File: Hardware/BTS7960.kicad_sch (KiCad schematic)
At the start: 29 parts, among them J10 Screw_Terminal_01x04, J11 Screw_Terminal_01x04, J4 Screw_Terminal_01x04, U7 HCPL-2631, U8 HCPL-2631

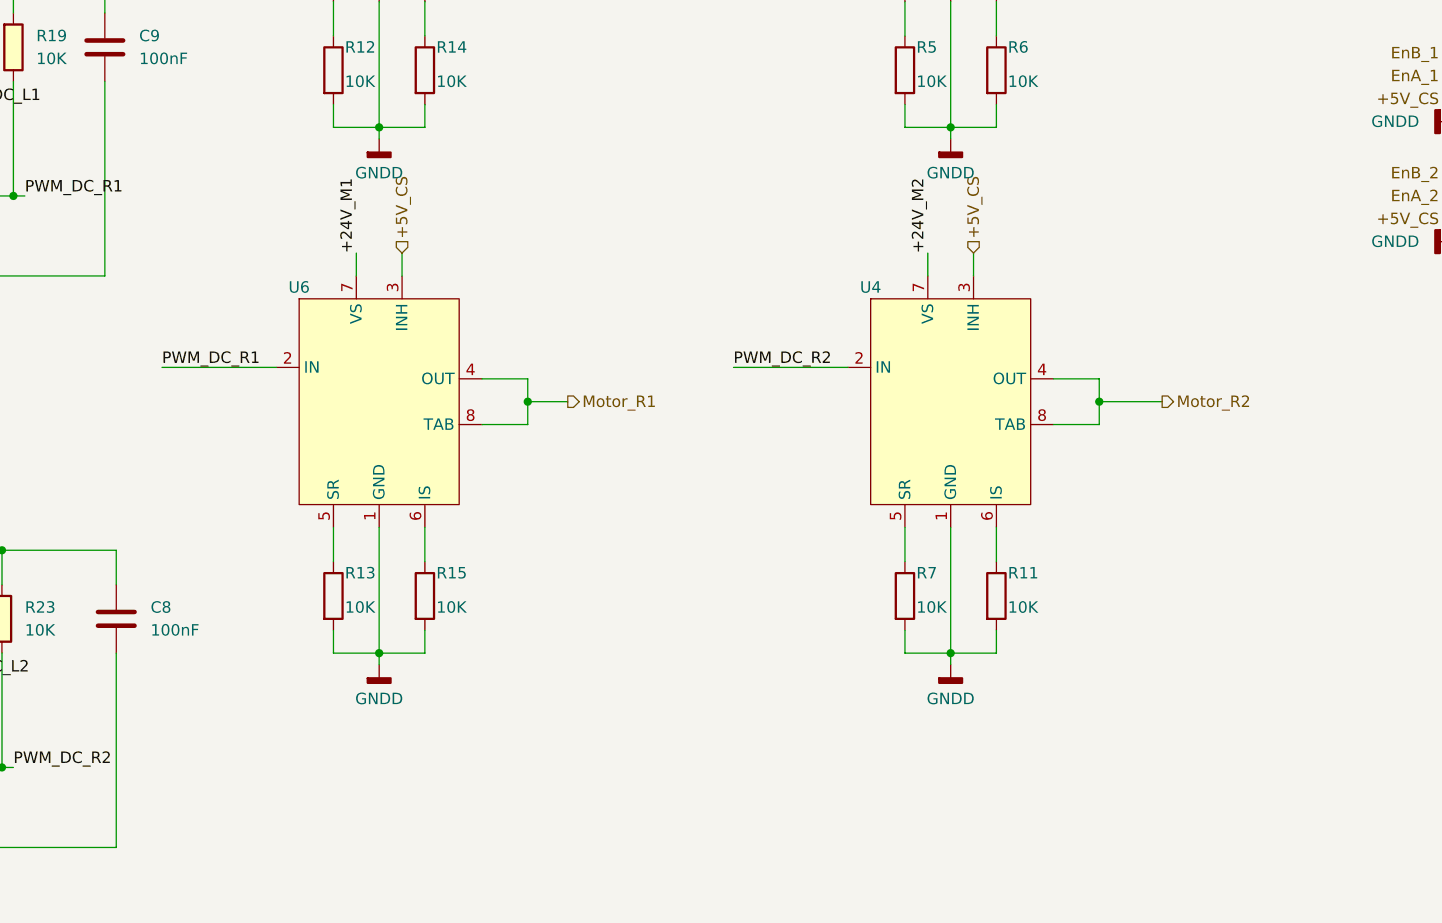
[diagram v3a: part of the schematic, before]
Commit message: Update schematic part2
Vẽ bus dành cho khối BLDC
Đóng khối chức năng cho sheet MCT8316
Tạo sheet nguồn cho các mạch nguồn Buck DCDC, LDO LD1117, BS0505
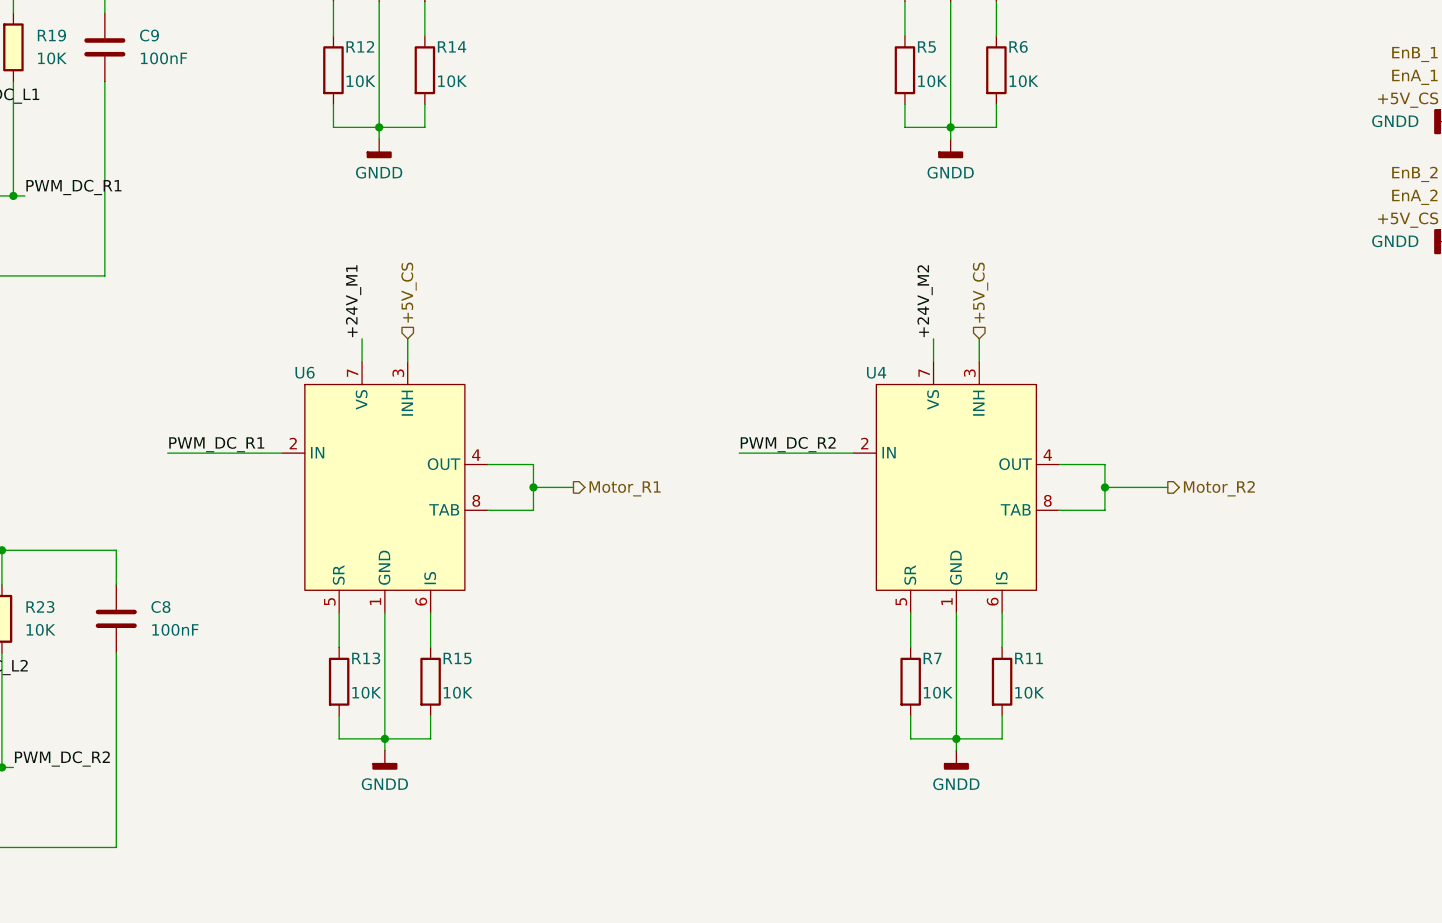
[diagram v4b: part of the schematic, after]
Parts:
- J10, J11: footprint Connector_PinHeader_2.54mm:PinHeader_1x04_P2.54mm_Vertical -> IVS_FOOTPRINTS:Conn-Vert-THT-4P-2.54mm-S4B_XH_SM4_TB
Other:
- moved on the sheet: R11, R13, R15, R7, U4, U6

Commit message: Add PCB
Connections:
- net MCU_PWM_L1: now also R16.1; no longer R17.1
- net MCU_PWM_R1: now also R17.1; no longer R16.1
- net PWM_DC_L1: now also R19.2, U7.6 (VO2); no longer R18.2, U7.7 (VO1)
- net PWM_DC_R1: now also R18.2, U7.7 (VO1); no longer R19.2, U7.6 (VO2)
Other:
- note added: "Driver Motor DC"
- note added: "Input Encoder"
- note added: "Isolation"
- note added: "Output Motor"
- moved on the sheet: C8, C9, F3, F4, J10, J11, J4, R11, R12, R13, R14, R15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

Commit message: Layout PCB
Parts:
- J4: footprint TerminalBlock:TerminalBlock_bornier-4_P5.08mm -> IVS_FOOTPRINTS:TerminalBlock_bornier-4_P5.08mm
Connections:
- net EnA_1 renamed En.EnA_1
- net EnA_2 renamed En.EnA_2
- net EnB_1 renamed En.EnB_1
- net EnB_2 renamed En.EnB_2
- net MCU_PWM_L1 renamed BTS.PWM_L1
- net MCU_PWM_L2 renamed BTS.PWM_L2
- net MCU_PWM_R1 renamed BTS.PWM_R1
- net MCU_PWM_R2 renamed BTS.PWM_R2
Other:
- moved on the sheet: C8, C9, F3, F4, R11, R12, R13, R14, R15, R16, R17, R18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

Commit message: Update Encoder
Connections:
- net +5V_CS: no longer J10.3 (Pin_3), J11.3 (Pin_3)
- net GND: now also J10.4 (Pin_4), J11.4 (Pin_4)
- net GNDD: no longer J10.4 (Pin_4), J11.4 (Pin_4)
- new net +3V3_MCU: J10.3 (Pin_3), J11.3 (Pin_3)
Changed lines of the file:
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@@
     (effects (font (size 1.27 1.27)) (justify left))
-  )
-  (hierarchical_label "+5V_CS" (shape input) (at 121.92 180.975 180) (fields_autoplaced)
-    (effects (font (size 1.27 1.27)) (justify right))
   )
   (hierarchical_label "En{En}" (shape output) (at 140.97 44.45 0) (fields_autoplaced)
@@
     (effects (font (size 1.27 1.27)) (justify left))
   )
+  (hierarchical_label "+3V3_MCU" (shape input) (at 121.92 180.975 180) (fields_autoplaced)
+    (effects (font (size 1.27 1.27)) (justify right))
+  )
   (hierarchical_label "+5V_CS" (shape input) (at 60.325 88.265 90) (fields_autoplaced)
     (effects (font (size 1.27 1.27)) (justify left))
@@
     (effects (font (size 1.27 1.27)) (justify left))
   )
-  (hierarchical_label "+5V_CS" (shape input) (at 121.92 167.64 180) (fields_autoplaced)
+  (hierarchical_label "+3V3_MCU" (shape input) (at 121.92 167.64 180) (fields_autoplaced)
     (effects (font (size 1.27 1.27)) (justify right))
   )
@@
     )
   )
+  (symbol (lib_id "power:GND") (at 121.92 183.515 270) (unit 1)
+    (in_bom yes) (on_board yes) (dnp no) (fields_autoplaced)
+    (property "Reference" "#PWR051" (at 115.57 183.515 0)
+      (effects (font (size 1.27 1.27)) hide)
+    )
+    (property "Value" "GND" (at 118.11 183.515 90)
+      (effects (font (size 1.27 1.27)) (justify right))
+    )
+    (property "Footprint" "" (at 121.92 183.515 0)
+      (effects (font (size 1.27 1.27)) hide)
+    )
+    (property "Datasheet" "" (at 121.92 183.515 0)
+      (effects (font (size 1.27 1.27)) hide)
+    )
+    (pin "1")
+    (instances
+      (project "DriverMotor"
+        (path "/8a82bd86-ff43-47ee-a4c0-46ff08914251/69bbd6ce-e9d0-4e66-98e2-7e43c19203ad"
+          (reference "#PWR051") (unit 1)
+        )
+      )
+    )
+  )
   (symbol (lib_name "BTS7960_2") (lib_id "IVS_SYMBOLS:BTS7960") (at 248.285 47.625 0) (unit 1)
     (in_bom yes) (on_board yes) (dnp no)
@@
     )
   )
-  (symbol (lib_id "power:GNDD") (at 121.92 183.515 270) (unit 1)
-    (in_bom yes) (on_board yes) (dnp no) (fields_autoplaced)
-    (property "Reference" "#PWR052" (at 115.57 183.515 0)
-      (effects (font (size 1.27 1.27)) hide)
-    )
-    (property "Value" "GNDD" (at 118.11 183.515 90)
-      (effects (font (size 1.27 1.27)) (justify right))
-    )
-    (property "Footprint" "" (at 121.92 183.515 0)
-      (effects (font (size 1.27 1.27)) hide)
-    )
-    (property "Datasheet" "" (at 121.92 183.515 0)
-      (effects (font (size 1.27 1.27)) hide)
-    )
-    (pin "1")
-    (instances
-      (project "DriverMotor"
-        (path "/8a82bd86-ff43-47ee-a4c0-46ff08914251/69bbd6ce-e9d0-4e66-98e2-7e43c19203ad"
-          (reference "#PWR052") (unit 1)
-        )
-      )
-    )
-  )
   (symbol (lib_id "power:GND") (at 50.165 50.165 270) (unit 1)
     (in_bom yes) (on_board yes) (dnp no) (fields_autoplaced)
@@
         (path "/8a82bd86-ff43-47ee-a4c0-46ff08914251/69bbd6ce-e9d0-4e66-98e2-7e43c19203ad"
           (reference "R19") (unit 1)
+        )
+      )
+    )
+  )
+  (symbol (lib_id "power:GND") (at 121.92 170.18 270) (unit 1)
+    (in_bom yes) (on_board yes) (dnp no) (fields_autoplaced)
+    (property "Reference" "#PWR047" (at 115.57 170.18 0)
+      (effects (font (size 1.27 1.27)) hide)
+    )
+    (property "Value" "GND" (at 118.11 170.18 90)
+      (effects (font (size 1.27 1.27)) (justify right))
+    )
+    (property "Footprint" "" (at 121.92 170.18 0)
+      (effects (font (size 1.27 1.27)) hide)
+    )
+    (property "Datasheet" "" (at 121.92 170.18 0)
+      (effects (font (size 1.27 1.27)) hide)
+    )
+    (pin "1")
+    (instances
+      (project "DriverMotor"
+        (path "/8a82bd86-ff43-47ee-a4c0-46ff08914251/69bbd6ce-e9d0-4e66-98e2-7e43c19203ad"
+          (reference "#PWR047") (unit 1)
         )
       )
@@
         )
       )
-    )
-  )
-  (symbol (lib_id "power:GNDD") (at 121.92 170.18 270) (unit 1)
-    (in_bom yes) (on_board yes) (dnp no) (fields_autoplaced)
-    (property "Reference" "#PWR051" (at 115.57 170.18 0)
-      (effects (font (size 1.27 1.27)) hide)
-    )
-    (property "Value" "GNDD" (at 118.11 170.18 90)
-      (effects (font (size 1.27 1.27)) (justify right))
-    )
-    (property "Footprint" "" (at 121.92 170.18 0)
-      (effects (font (size 1.27 1.27)) hide)
-    )
-    (property "Datasheet" "" (at 121.92 170.18 0)
-      (effects (font (size 1.27 1.27)) hide)
-    )
-    (pin "1")
-    (instances
-      (project "DriverMotor"
-        (path "/8a82bd86-ff43-47ee-a4c0-46ff08914251/69bbd6ce-e9d0-4e66-98e2-7e43c19203ad"
-          (reference "#PWR051") (unit 1)
-        )
-      )

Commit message: Fix bug schematic
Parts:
- J10, J11: symbol Connector:Screw_Terminal_01x04 -> Connector:Conn_01x04_Pin
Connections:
- net +3V3_MCU renamed +5V
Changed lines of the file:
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@@
     (stroke (width 0) (type default))
   )
-  (wire (pts (xy 121.92 167.64) (xy 130.81 167.64))
+  (wire (pts (xy 139.065 167.64) (xy 147.955 167.64))
     (stroke (width 0) (type default))
   )
@@
     (stroke (width 0) (type default))
   )
-  (wire (pts (xy 121.92 183.515) (xy 130.81 183.515))
+  (wire (pts (xy 139.065 183.515) (xy 147.955 183.515))
     (stroke (width 0) (type default))
   )
@@
     (stroke (width 0) (type default))
   )
-  (wire (pts (xy 121.92 175.895) (xy 130.81 175.895))
+  (wire (pts (xy 139.065 175.895) (xy 147.955 175.895))
     (stroke (width 0) (type default))
   )
@@
     (stroke (width 0) (type default))
   )
-  (wire (pts (xy 121.92 165.1) (xy 130.81 165.1))
+  (wire (pts (xy 139.065 165.1) (xy 147.955 165.1))
     (stroke (width 0) (type default))
   )
@@
     (stroke (width 0) (type default))
   )
-  (wire (pts (xy 121.92 162.56) (xy 130.81 162.56))
+  (wire (pts (xy 139.065 162.56) (xy 147.955 162.56))
     (stroke (width 0) (type default))
   )
@@
     (stroke (width 0) (type default))
   )
-  (wire (pts (xy 121.92 178.435) (xy 130.81 178.435))
+  (wire (pts (xy 139.065 178.435) (xy 147.955 178.435))
     (stroke (width 0) (type default))
   )
@@
     (stroke (width 0) (type default))
   )
-  (wire (pts (xy 121.92 170.18) (xy 130.81 170.18))
+  (wire (pts (xy 139.065 170.18) (xy 147.955 170.18))
     (stroke (width 0) (type default))
   )
@@
     (stroke (width 0) (type default))
   )
-  (wire (pts (xy 121.92 180.975) (xy 130.81 180.975))
+  (wire (pts (xy 139.065 180.975) (xy 147.955 180.975))
     (stroke (width 0) (type default))
   )
@@
     (fill (type none))
   )
-  (rectangle (start 107.95 159.385) (end 161.925 194.31)
+  (rectangle (start 99.06 159.385) (end 161.925 194.31)
     (stroke (width 0) (type default))
     (fill (type none))
@@
     (effects (font (size 1.27 1.27)) (justify left bottom))
   )
-  (label "En.EnB_1" (at 121.92 162.56 180) (fields_autoplaced)
+  (label "En.EnB_1" (at 139.065 162.56 180) (fields_autoplaced)
     (effects (font (size 1.27 1.27)) (justify right bottom))
   )
@@
     (effects (font (size 1.27 1.27)) (justify right bottom))
   )
-  (label "En.EnA_1" (at 121.92 165.1 180) (fields_autoplaced)
+  (label "En.EnA_1" (at 139.065 165.1 180) (fields_autoplaced)
     (effects (font (size 1.27 1.27)) (justify right bottom))
   )
@@
     (effects (font (size 1.27 1.27)) (justify right bottom))
   )
-  (label "En.EnA_2" (at 121.92 178.435 180) (fields_autoplaced)
+  (label "En.EnA_2" (at 139.065 178.435 180) (fields_autoplaced)
     (effects (font (size 1.27 1.27)) (justify right bottom))
   )
@@
     (effects (font (size 1.27 1.27)) (justify right bottom))
   )
-  (label "En.EnB_2" (at 121.92 175.895 180) (fields_autoplaced)
+  (label "En.EnB_2" (at 139.065 175.895 180) (fields_autoplaced)
     (effects (font (size 1.27 1.27)) (justify right bottom))
   )
@@
     (effects (font (size 1.27 1.27)) (justify left))
   )
-  (hierarchical_label "+3V3_MCU" (shape input) (at 121.92 180.975 180) (fields_autoplaced)
-    (effects (font (size 1.27 1.27)) (justify right))
-  )
   (hierarchical_label "+5V_CS" (shape input) (at 60.325 88.265 90) (fields_autoplaced)
     (effects (font (size 1.27 1.27)) (justify left))
@@
     (effects (font (size 1.27 1.27)) (justify left))
   )
-  (hierarchical_label "+3V3_MCU" (shape input) (at 121.92 167.64 180) (fields_autoplaced)
-    (effects (font (size 1.27 1.27)) (justify right))
-  )
   (hierarchical_label "Motor_L2" (shape input) (at 50.165 168.275 180) (fields_autoplaced)
     (effects (font (size 1.27 1.27)) (justify right))
@@
     )
   )
-  (symbol (lib_id "Connector:Screw_Terminal_01x04") (at 135.89 165.1 0) (unit 1)
-    (in_bom yes) (on_board yes) (dnp no) (fields_autoplaced)
-    (property "Reference" "J10" (at 138.43 165.1 0)
-      (effects (font (size 1.27 1.27)) (justify left))
-    )
-    (property "Value" "Screw_Terminal_01x04" (at 138.43 167.64 0)
-      (effects (font (size 1.27 1.27)) (justify left))
-    )
-    (property "Footprint" "IVS_FOOTPRINTS:Conn-Vert-THT-4P-2.54mm-S4B_XH_SM4_TB" (at 135.89 165.1 0)
-      (effects (font (size 1.27 1.27)) hide)
-    )
-    (property "Datasheet" "~" (at 135.89 165.1 0)
+  (symbol (lib_id "Connector:Conn_01x04_Pin") (at 153.035 165.1 0) (mirror y) (unit 1)
+    (in_bom yes) (on_board yes) (dnp no)
+    (property "Reference" "J10" (at 157.48 165.1 0)
+      (effects (font (size 1.27 1.27)) (justify left))
+    )
+    (property "Value" "Screw_Terminal_01x04" (at 175.26 169.545 0)
+      (effects (font (size 1.27 1.27)) (justify left) hide)
+    )
+    (property "Footprint" "IVS_FOOTPRINTS:Conn-Vert-THT-4P-2.54mm-S4B_XH_SM4_TB" (at 153.035 165.1 0)
+      (effects (font (size 1.27 1.27)) hide)
+    )
+    (property "Datasheet" "~" (at 153.035 165.1 0)
       (effects (font (size 1.27 1.27)) hide)
     )
@@
     )
   )
-  (symbol (lib_id "power:GND") (at 121.92 183.515 270) (unit 1)
-    (in_bom yes) (on_board yes) (dnp no) (fields_autoplaced)
-    (property "Reference" "#PWR051" (at 115.57 183.515 0)
-      (effects (font (size 1.27 1.27)) hide)
-    )
-    (property "Value" "GND" (at 118.11 183.515 90)
+  (symbol (lib_id "power:GND") (at 139.065 183.515 270) (unit 1)
+    (in_bom yes) (on_board yes) (dnp no) (fields_autoplaced)
+    (property "Reference" "#PWR051" (at 132.715 183.515 0)
+      (effects (font (size 1.27 1.27)) hide)
+    )
+    (property "Value" "GND" (at 135.255 183.515 90)
       (effects (font (size 1.27 1.27)) (justify right))
     )
-    (property "Footprint" "" (at 121.92 183.515 0)
-      (effects (font (size 1.27 1.27)) hide)
-    )
-    (property "Datasheet" "" (at 121.92 183.515 0)
+    (property "Footprint" "" (at 139.065 183.515 0)
+      (effects (font (size 1.27 1.27)) hide)
+    )
+    (property "Datasheet" "" (at 139.065 183.515 0)
       (effects (font (size 1.27 1.27)) hide)
     )
@@
     )
   )
-  (symbol (lib_id "Connector:Screw_Terminal_01x04") (at 135.89 178.435 0) (unit 1)
-    (in_bom yes) (on_board yes) (dnp no) (fields_autoplaced)
-    (property "Reference" "J11" (at 138.43 178.435 0)
-      (effects (font (size 1.27 1.27)) (justify left))
-    )
-    (property "Value" "Screw_Terminal_01x04" (at 138.43 180.975 0)
-      (effects (font (size 1.27 1.27)) (justify left))
-    )
-    (property "Footprint" "IVS_FOOTPRINTS:Conn-Vert-THT-4P-2.54mm-S4B_XH_SM4_TB" (at 135.89 178.435 0)
-      (effects (font (size 1.27 1.27)) hide)
-    )
-    (property "Datasheet" "~" (at 135.89 178.435 0)
+  (symbol (lib_id "Connector:Conn_01x04_Pin") (at 153.035 178.435 0) (mirror y) (unit 1)
+    (in_bom yes) (on_board yes) (dnp no)
+    (property "Reference" "J11" (at 156.845 175.26 0)
+      (effects (font (size 1.27 1.27)) (justify left))
+    )
+    (property "Value" "Screw_Terminal_01x04" (at 150.495 180.975 0)
+      (effects (font (size 1.27 1.27)) (justify left) hide)
+    )
+    (property "Footprint" "IVS_FOOTPRINTS:Conn-Vert-THT-4P-2.54mm-S4B_XH_SM4_TB" (at 153.035 178.435 0)
+      (effects (font (size 1.27 1.27)) hide)
+    )
+    (property "Datasheet" "~" (at 153.035 178.435 0)
       (effects (font (size 1.27 1.27)) hide)
     )
@@
         (path "/8a82bd86-ff43-47ee-a4c0-46ff08914251/69bbd6ce-e9d0-4e66-98e2-7e43c19203ad"
           (reference "J11") (unit 1)
+        )
+      )
+    )
+  )
+  (symbol (lib_id "power:+5V") (at 139.065 167.64 90) (unit 1)
+    (in_bom yes) (on_board yes) (dnp no) (fields_autoplaced)
+    (property "Reference" "#PWR052" (at 142.875 167.64 0)
+      (effects (font (size 1.27 1.27)) hide)
+    )
+    (property "Value" "+5V" (at 135.89 167.64 90)
+      (effects (font (size 1.27 1.27)) (justify left))
+    )
+    (property "Footprint" "" (at 139.065 167.64 0)
+      (effects (font (size 1.27 1.27)) hide)
+    )
+    (property "Datasheet" "" (at 139.065 167.64 0)
+      (effects (font (size 1.27 1.27)) hide)
+    )
+    (pin "1")
+    (instances
+      (project "DriverMotor"
+        (path "/8a82bd86-ff43-47ee-a4c0-46ff08914251/69bbd6ce-e9d0-4e66-98e2-7e43c19203ad"
+          (reference "#PWR052") (unit 1)
         )
       )
@@
     )
   )
-  (symbol (lib_id "power:GND") (at 121.92 170.18 270) (unit 1)
-    (in_bom yes) (on_board yes) (dnp no) (fields_autoplaced)
-    (property "Reference" "#PWR047" (at 115.57 170.18 0)
-      (effects (font (size 1.27 1.27)) hide)
-    )
-    (property "Value" "GND" (at 118.11 170.18 90)
+  (symbol (lib_id "power:GND") (at 139.065 170.18 270) (unit 1)
+    (in_bom yes) (on_board yes) (dnp no) (fields_autoplaced)
+    (property "Reference" "#PWR047" (at 132.715 170.18 0)
+      (effects (font (size 1.27 1.27)) hide)
+    )
+    (property "Value" "GND" (at 135.255 170.18 90)
       (effects (font (size 1.27 1.27)) (justify right))
     )
-    (property "Footprint" "" (at 121.92 170.18 0)
-      (effects (font (size 1.27 1.27)) hide)
-    )
-    (property "Datasheet" "" (at 121.92 170.18 0)
+    (property "Footprint" "" (at 139.065 170.18 0)
+      (effects (font (size 1.27 1.27)) hide)
+    )
+    (property "Datasheet" "" (at 139.065 170.18 0)
       (effects (font (size 1.27 1.27)) hide)
     )
@@
         )
       )
+    )
+  )
+  (symbol (lib_id "power:+5V") (at 139.065 180.975 90) (unit 1)
+    (in_bom yes) (on_board yes) (dnp no) (fields_autoplaced)
+    (property "Reference" "#PWR056" (at 142.875 180.975 0)
+      (effects (font (size 1.27 1.27)) hide)
+    )
+    (property "Value" "+5V" (at 135.89 180.975 90)
+      (effects (font (size 1.27 1.27)) (justify left))
+    )
+    (property "Footprint" "" (at 139.065 180.975 0)
+      (effects (font (size 1.27 1.27)) hide)
+    )
+    (property "Datasheet" "" (at 139.065 180.975 0)
+      (effects (font (size 1.27 1.27)) hide)
+    )
+    (pin "1")
+    (instances
+      (project "DriverMotor"
+        (path "/8a82bd86-ff43-47ee-a4c0-46ff08914251/69bbd6ce-e9d0-4e66-98e2-7e43c19203ad"
+          (reference "#PWR056") (unit 1)
+        )
+      )
